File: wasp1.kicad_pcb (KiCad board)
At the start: 2 copper layers, 162.6 x 175.3 mm, 46 parts

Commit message: Cutouts
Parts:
- removed the REF** at (102.8, 175.3)
- moved REF** 9.56 mm to (127.0, 129.1)
- moved REF** 9.56 mm to (149.8, 129.1)
- moved REF** 9.56 mm to (157.5, 157.0)
- moved REF** 9.56 mm to (157.5, 136.7)
- moved REF** 9.56 mm to (109.2, 131.6)
- moved REF** 8.48 mm to (16.4, 167.2)
- moved REF** 8.48 mm to (76.2, 136.7)
- moved REF** 8.48 mm to (68.6, 129.1)
- moved REF** 8.48 mm to (76.2, 157.0)
- moved REF** 8.48 mm to (45.7, 129.1)
- moved REF** 8.48 mm to (27.9, 131.6)
- moved REF** 7.18 mm to (147.3, 38.1)
- moved REF** 7.18 mm to (139.7, 17.8)
- moved REF** 7.18 mm to (147.3, 78.7)
- moved REF** 7.18 mm to (127.0, 38.1)
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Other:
- board size 162.6 x 175.3 mm -> 160 x 160 mm

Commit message: All components
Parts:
- removed the REF** at (111.8, 99.1)
- removed the REF** at (142.2, 58.4)
- removed the REF** at (160.0, 17.8)
- removed the REF** at (119.4, 17.8)
- removed the REF** at (116.8, 116.8)
- removed the REF** at (40.6, 58.4)
- removed the REF** at (132.1, 99.1)
- removed the REF** at (38.1, 17.8)
- removed the REF** at (106.7, 78.7)
- removed the REF** at (45.7, 38.1)
- removed the REF** at (61.0, 58.4)
- removed the REF** at (20.3, 58.4)
- removed the REF** at (127.0, 129.1)
- removed the REF** at (147.3, 38.1)
- removed the REF** at (139.7, 17.8)
- removed the REF** at (106.7, 38.1)
- removed the REF** at (25.4, 38.1)
- removed the REF** at (149.8, 129.1)
- removed the REF** at (147.3, 78.7)
- removed the REF** at (58.4, 17.8)
- removed the REF** at (127.0, 38.1)
- removed the REF** at (66.0, 78.7)
- removed the REF** at (121.9, 58.4)
- removed the REF** at (78.7, 17.8)
- removed the REF** at (76.2, 157.0)
- removed the REF** at (101.6, 58.4)
- removed the REF** at (25.4, 78.7)
- removed the REF** at (139.7, 116.8)
- removed the REF** at (152.4, 99.1)
- removed the REF** at (127.0, 78.7)
- removed the REF** at (157.5, 157.0)
- removed the REF** at (157.5, 136.7)
- removed the REF** at (66.0, 38.1)
- removed the REF** at (45.7, 78.7)
- added REF**: SW_Cherry_MX_1.00u_PCB, Button_Switch_Keyboard:SW_Cherry_MX_1.00u_PCB, F.Cu at (149.8, 73.1)
- added REF**: SW_Cherry_MX_1.00u_PCB, Button_Switch_Keyboard:SW_Cherry_MX_1.00u_PCB, F.Cu at (168.8, 60.4)
- added REF**: SW_Cherry_MX_1.00u_PCB, Button_Switch_Keyboard:SW_Cherry_MX_1.00u_PCB, F.Cu at (41.2, 108.9)
- added REF**: SW_Cherry_MX_1.00u_PCB, Button_Switch_Keyboard:SW_Cherry_MX_1.00u_PCB, F.Cu at (130.8, 62.2)
- added REF**: SW_Cherry_MX_1.00u_PCB, Button_Switch_Keyboard:SW_Cherry_MX_1.00u_PCB, F.Cu at (149.8, 54.0)
- added REF**: SW_Cherry_MX_1.00u_PCB, Button_Switch_Keyboard:SW_Cherry_MX_1.00u_PCB, F.Cu at (130.8, 43.3)
- added REF**: SW_Cherry_MX_1.00u_PCB, Button_Switch_Keyboard:SW_Cherry_MX_1.00u_PCB, F.Cu at (55.8, 94.3)
- added REF**: SW_Cherry_MX_1.00u_PCB, Button_Switch_Keyboard:SW_Cherry_MX_1.00u_PCB, F.Cu at (111.7, 54.6)
- added REF**: SW_Cherry_MX_1.00u_PCB, Button_Switch_Keyboard:SW_Cherry_MX_1.00u_PCB, B.Cu at (64.2, 143.3)
- added REF**: SW_Cherry_MX_1.00u_PCB, Button_Switch_Keyboard:SW_Cherry_MX_1.00u_PCB, F.Cu at (92.7, 33.9)
- added REF**: SW_Cherry_MX_1.00u_PCB, Button_Switch_Keyboard:SW_Cherry_MX_1.00u_PCB, B.Cu at (64.2, 181.4)
- added REF**: SW_Cherry_MX_1.00u_PCB, Button_Switch_Keyboard:SW_Cherry_MX_1.00u_PCB, B.Cu at (26.1, 160.5)
- added REF**: SW_Cherry_MX_1.00u_PCB, Button_Switch_Keyboard:SW_Cherry_MX_1.00u_PCB, B.Cu at (64.2, 162.3)
- added REF**: SW_Cherry_MX_1.00u_PCB, Button_Switch_Keyboard:SW_Cherry_MX_1.00u_PCB, B.Cu at (45.1, 135.1)
- added REF**: SW_Cherry_MX_1.00u_PCB, Button_Switch_Keyboard:SW_Cherry_MX_1.00u_PCB, B.Cu at (45.1, 154.0)
- added REF**: SW_Cherry_MX_1.00u_PCB, Button_Switch_Keyboard:SW_Cherry_MX_1.00u_PCB, B.Cu at (83.2, 173.8)
- added REF**: PinHeader_2x05_P2.54mm_Horizontal, Connector_PinHeader_2.54mm:PinHeader_2x05_P2.54mm_Horizontal, B.Cu at (75.8, 43.7)
- added REF**: SW_Cherry_MX_1.00u_PCB, Button_Switch_Keyboard:SW_Cherry_MX_1.00u_PCB, F.Cu at (92.7, 72.0)
- added REF**: SW_Cherry_MX_1.00u_PCB, Button_Switch_Keyboard:SW_Cherry_MX_1.00u_PCB, B.Cu at (26.1, 141.3)
- added REF**: SW_Cherry_MX_1.00u_PCB, Button_Switch_Keyboard:SW_Cherry_MX_1.00u_PCB, B.Cu at (45.1, 173.2)
- added REF**: SW_Cherry_MX_1.00u_PCB, Button_Switch_Keyboard:SW_Cherry_MX_1.00u_PCB, B.Cu at (83.2, 135.7)
- added REF**: PinHeader_2x05_P2.54mm_Horizontal, Connector_PinHeader_2.54mm:PinHeader_2x05_P2.54mm_Horizontal, B.Cu at (75.8, 66.6)
- added REF**: SW_Cherry_MX_1.00u_PCB, Button_Switch_Keyboard:SW_Cherry_MX_1.00u_PCB, B.Cu at (83.2, 154.7)
- added REF**: SW_Cherry_MX_1.00u_PCB, Button_Switch_Keyboard:SW_Cherry_MX_1.00u_PCB, F.Cu at (168.8, 41.3)
- added REF**: SW_Cherry_MX_1.00u_PCB, Button_Switch_Keyboard:SW_Cherry_MX_1.00u_PCB, B.Cu at (161.3, 107.1)
- added REF**: PinHeader_2x05_P2.54mm_Horizontal, Connector_PinHeader_2.54mm:PinHeader_2x05_P2.54mm_Horizontal, B.Cu at (63.6, 53.9)
- added REF**: PinHeader_2x05_P2.54mm_Horizontal, Connector_PinHeader_2.54mm:PinHeader_2x05_P2.54mm_Horizontal, B.Cu at (63.6, 76.7)
- added REF**: SW_Cherry_MX_1.00u_PCB, Button_Switch_Keyboard:SW_Cherry_MX_1.00u_PCB, F.Cu at (111.7, 73.7)
- added REF**: SW_Cherry_MX_1.00u_PCB, Button_Switch_Keyboard:SW_Cherry_MX_1.00u_PCB, F.Cu at (149.8, 35.0)
- added REF**: SW_Cherry_MX_1.00u_PCB, Button_Switch_Keyboard:SW_Cherry_MX_1.00u_PCB, F.Cu at (130.8, 81.4)
- added REF**: SW_Cherry_MX_1.00u_PCB, Button_Switch_Keyboard:SW_Cherry_MX_1.00u_PCB, F.Cu at (92.7, 52.9)
- added REF**: SW_Cherry_MX_1.00u_PCB, Button_Switch_Keyboard:SW_Cherry_MX_1.00u_PCB, F.Cu at (111.7, 35.6)
- REF** (x3): moved to B.Cu
- moved REF** 137.8 mm to (153.0, 185.4), turned to 0 degrees
- moved REF** 120.2 mm to (52.1, 25.8), turned to 0 degrees
- moved REF** 118.1 mm to (134.0, 183.5), turned to 0 degrees
- moved REF** 102.4 mm to (102.2, 172.1), turned to -90 degrees
- moved REF** 96.9 mm to (119.2, 165.7), turned to 0 degrees
- moved REF** 89.7 mm to (131.4, 155.5), turned to 180 degrees
- moved REF** 74.5 mm to (102.2, 153.0), turned to -90 degrees
- moved REF** 72.1 mm to (146.7, 121.7), turned to 45 degrees
- moved REF** 64.3 mm to (119.2, 137.8), turned to 0 degrees
- moved REF** 62.9 mm to (131.4, 127.6), turned to 180 degrees
- moved REF** 46.8 mm to (102.2, 134.0), turned to -90 degrees
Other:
- board size 160 x 160 mm -> 156.1 x 167.7 mm
- board text added: "PinHeader_2x05_P2.54mm_Horizontal"

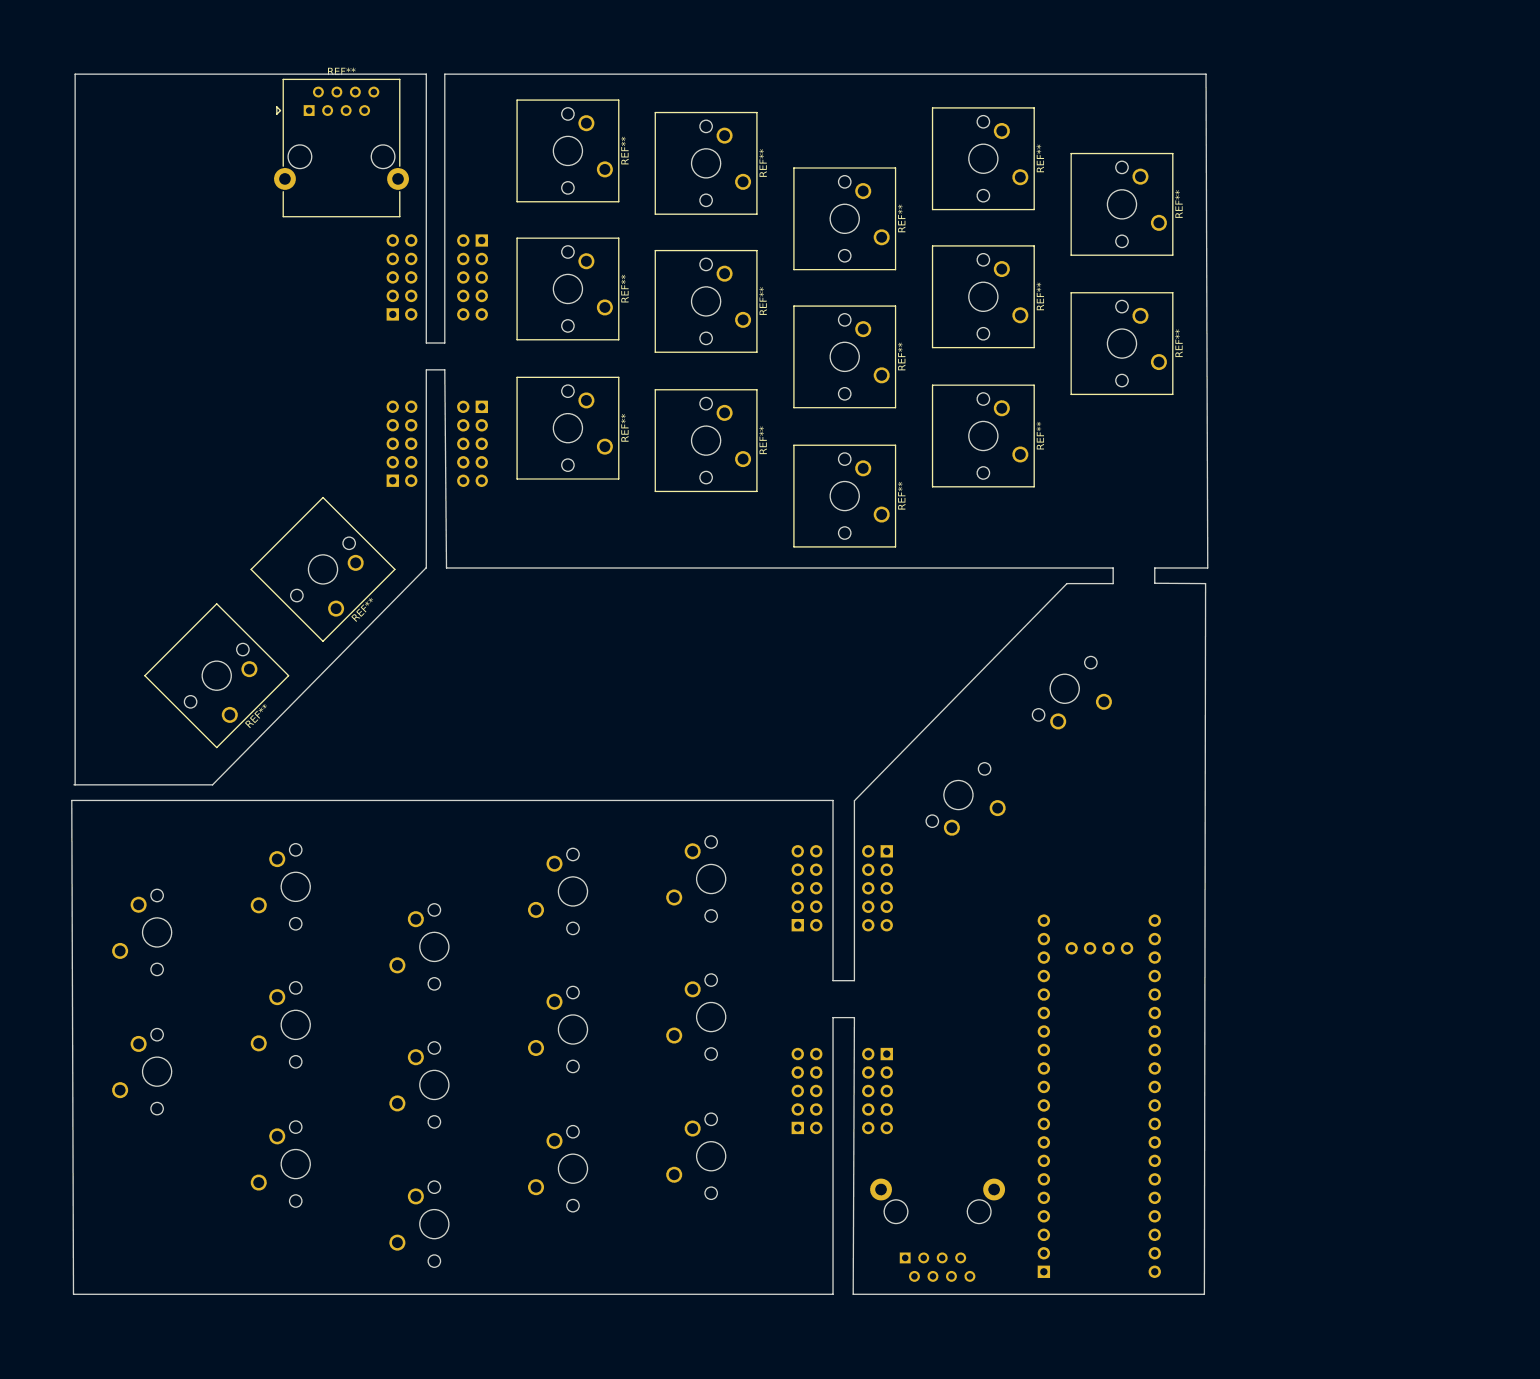
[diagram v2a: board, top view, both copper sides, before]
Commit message: Named everything and fixed some directions
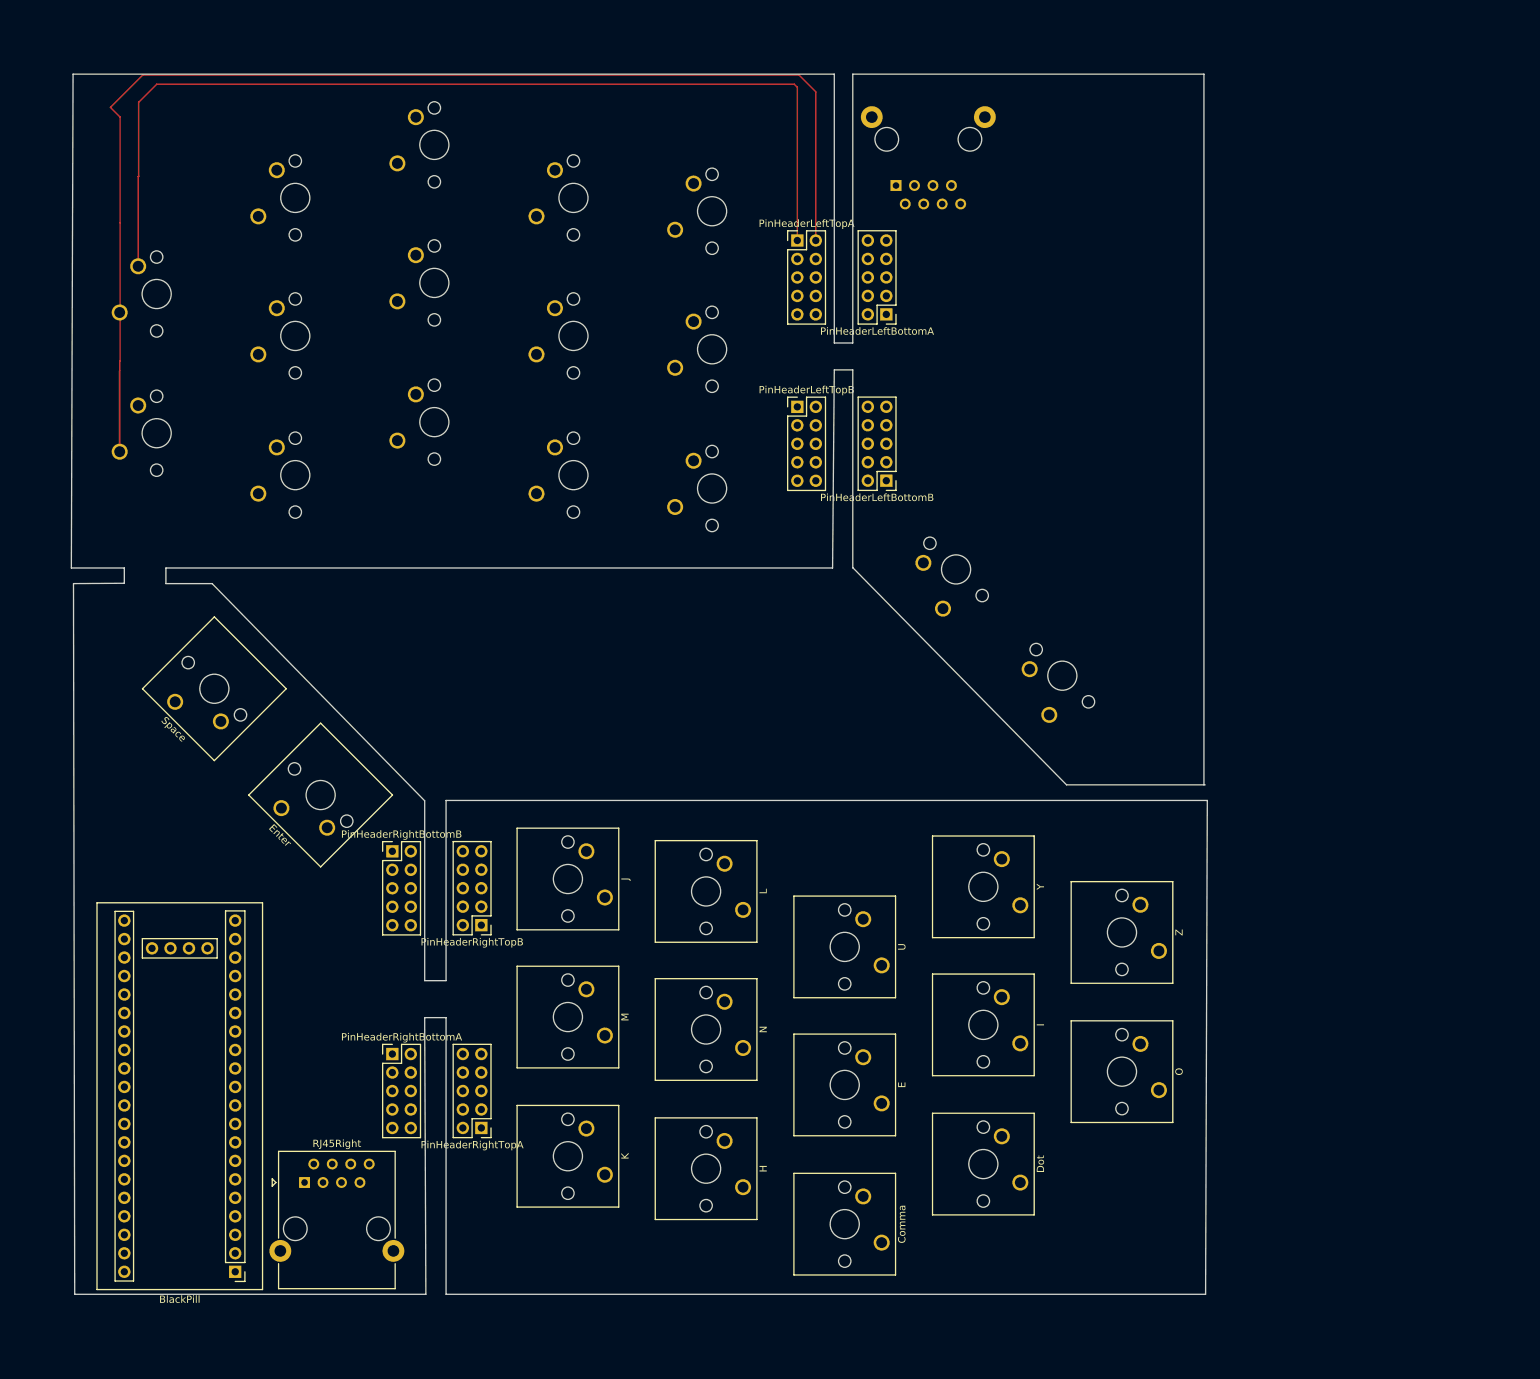
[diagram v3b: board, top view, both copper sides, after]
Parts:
- A, B, BackSpace, C, D, F, G, P, Q, R, RJ45Left, S, T, Tab, V, W, X: renamed from REF**; moved to B.Cu
- BlackPill, Comma, Dot, E, Enter, H, I, J, K, L, M, N, O, RJ45Right, Space, U, Y, Z: renamed from REF**; moved to F.Cu
- PinHeaderLeftBottomA, PinHeaderLeftBottomB, PinHeaderLeftTopA, PinHeaderLeftTopB, PinHeaderRightBottomA, PinHeaderRightBottomB, PinHeaderRightTopA, PinHeaderRightTopB: renamed from REF**; value PinHeader_2x05_P2.54mm_Horizontal -> PinHeader_2x05_P2.54mm_Vertical; footprint Connector_PinHeader_2.54mm:PinHeader_2x05_P2.54mm_Horizontal -> Connector_PinHeader_2.54mm:PinHeader_2x05_P2.54mm_Vertical; moved to F.Cu
- moved A 143.3 mm to (26.0, 72.7)
- moved Q 143.3 mm to (26.0, 53.6)
- moved O 142.8 mm to (168.8, 160.5)
- moved Z 142.8 mm to (168.8, 141.3)
- moved Space 127.6 mm to (33.7, 107.1), turned to 135 degrees
- moved BackSpace 112.6 mm to (153.8, 108.9), turned to -45 degrees
- moved BlackPill 111.1 mm to (41.9, 185.4), turned to 180 degrees
- moved R 104.9 mm to (45.1, 59.4)
- moved W 104.9 mm to (45.1, 40.4)
- moved X 104.9 mm to (45.1, 78.5)
- moved Dot 104.7 mm to (149.8, 173.2)
- moved I 104.7 mm to (149.8, 154.0)
- moved Y 104.7 mm to (149.8, 135.1)
- moved Enter 98.4 mm to (48.3, 121.7), turned to 135 degrees
- moved Tab 83.4 mm to (139.2, 94.3), turned to -45 degrees
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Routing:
- net (no net): track 0.00 -> 303.5 mm
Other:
- outline, holes or cut-outs redrawn
